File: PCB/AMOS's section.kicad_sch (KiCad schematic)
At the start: 17 parts, among them J1 USB_C_Receptacle_PowerOnly_6P, J2 Conn_02x16_Odd_Even, U6 TP4056-42-ESOP8, U7 CH224K, U8 TS5A3159ADBVR

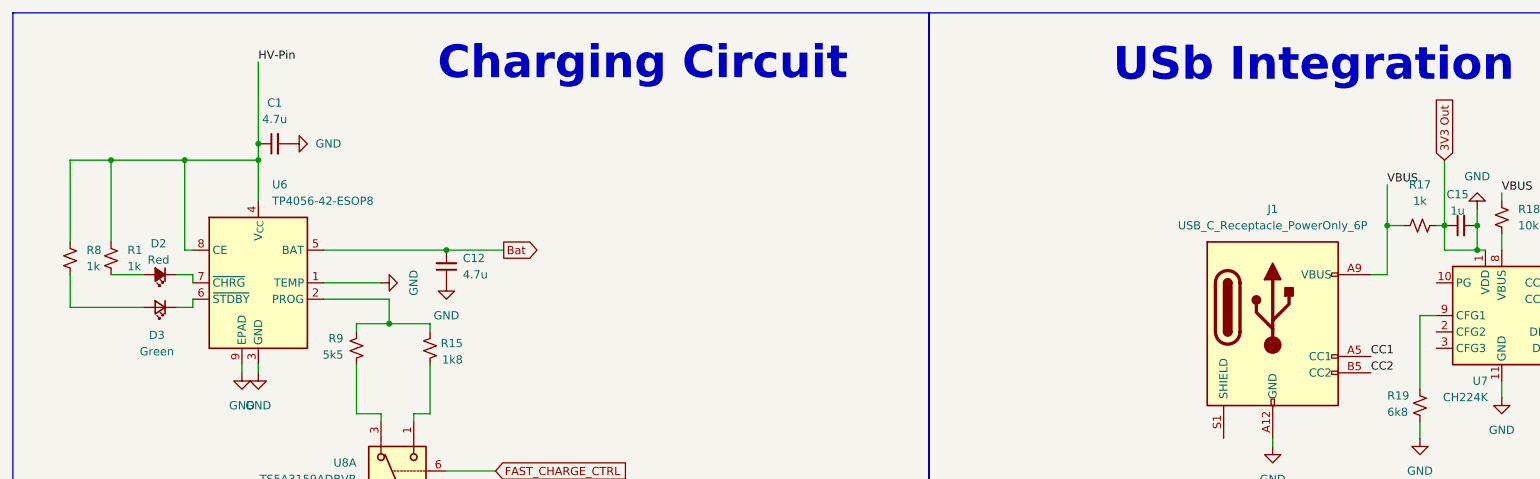
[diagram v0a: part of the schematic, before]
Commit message: Add footprint for charging circuit and usb integration
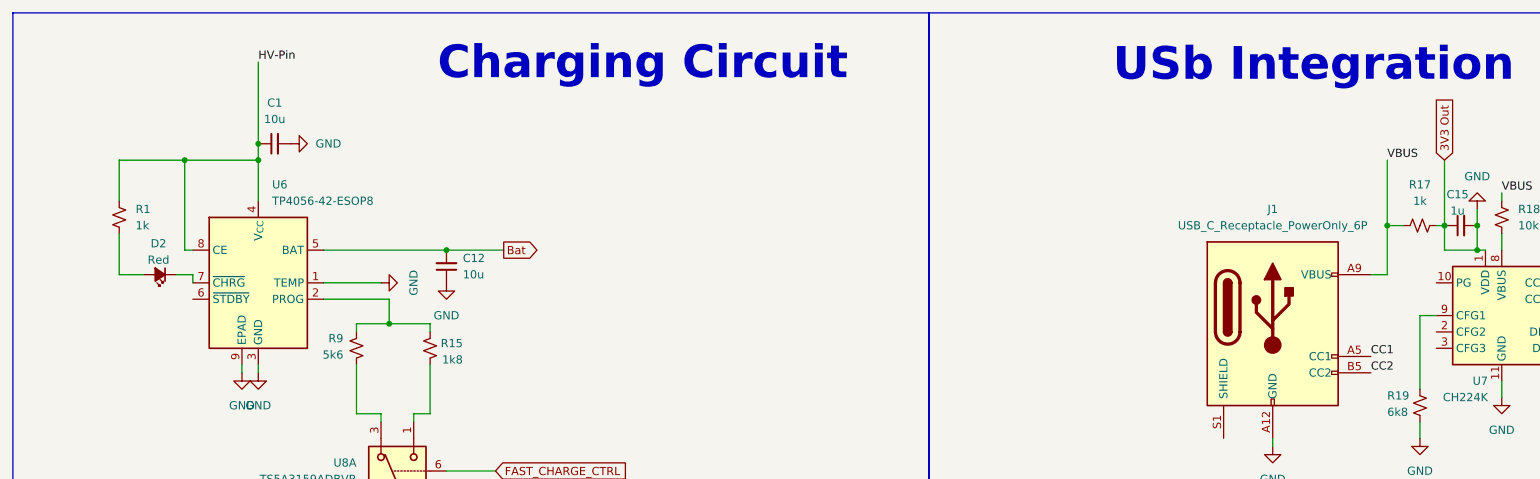
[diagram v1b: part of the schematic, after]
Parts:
- removed D3: Green, symbol Device:LED_Small
- removed R8: 1k, symbol Device:R_Small_US
- C1, C12: value 4.7u -> 10u; footprint (none) -> Nhlamolo.:C1206; LSCS (none) -> C13585
- C15: footprint (none) -> Nhlamolo.:C1206; LSCS (none) -> C1848
- D2: footprint (none) -> Nhlamolo.:LED0603-RD; LCSC (none) -> C2286
- J1: footprint Connector_USB:USB_C_Receptacle_HCTL_HC-TYPE-C-16P-01A -> Nhlamolo.:USB-C-SMD_TYPE-602-T3; LSCS (none) -> C2927028
- R1: footprint (none) -> Nhlamolo.:R0402; LCSC (none) -> C11702
- R15: footprint (none) -> Nhlamolo.:R0603; LSCS (none) -> C4177
- R17: footprint (none) -> Nhlamolo.:R0402; LSCS (none) -> C11702
- R18: footprint (none) -> Nhlamolo.:R0805; LSCS (none) -> C17414
- R19: footprint (none) -> Nhlamolo.:R0805; LSCS (none) -> C17772
- R9: value 5k5 -> 5k6; footprint (none) -> Nhlamolo.:R0805; LSCS (none) -> C4382
- U6: footprint Package_SO:SOIC-8-1EP_3.9x4.9mm_P1.27mm_EP2.41x3.3mm_ThermalVias -> Nhlamolo.:ESOP-8_L4.9-W3.9-P1.27-LS6.0-BL-EP-1; LCSC (none) -> C16581
- U7: footprint Package_SO:SSOP-10-1EP_3.9x4.9mm_P1mm_EP2.1x3.3mm -> Nhlamolo.:ESSOP-10_L4.9-W3.9-P1.0-LS6.0-TL-EP; LSCS (none) -> C970725
- U8: footprint Package_TO_SOT_SMD:SOT-23-6 -> Nhlamolo.:SOT-23-6_L2.9-W1.6-P0.95-LS2.8-BR; LSCS (none) -> C128405
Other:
- moved on the sheet: R1
